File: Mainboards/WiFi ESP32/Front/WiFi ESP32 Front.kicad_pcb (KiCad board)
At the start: 2 copper layers, 71.5 x 24 mm, 8 parts

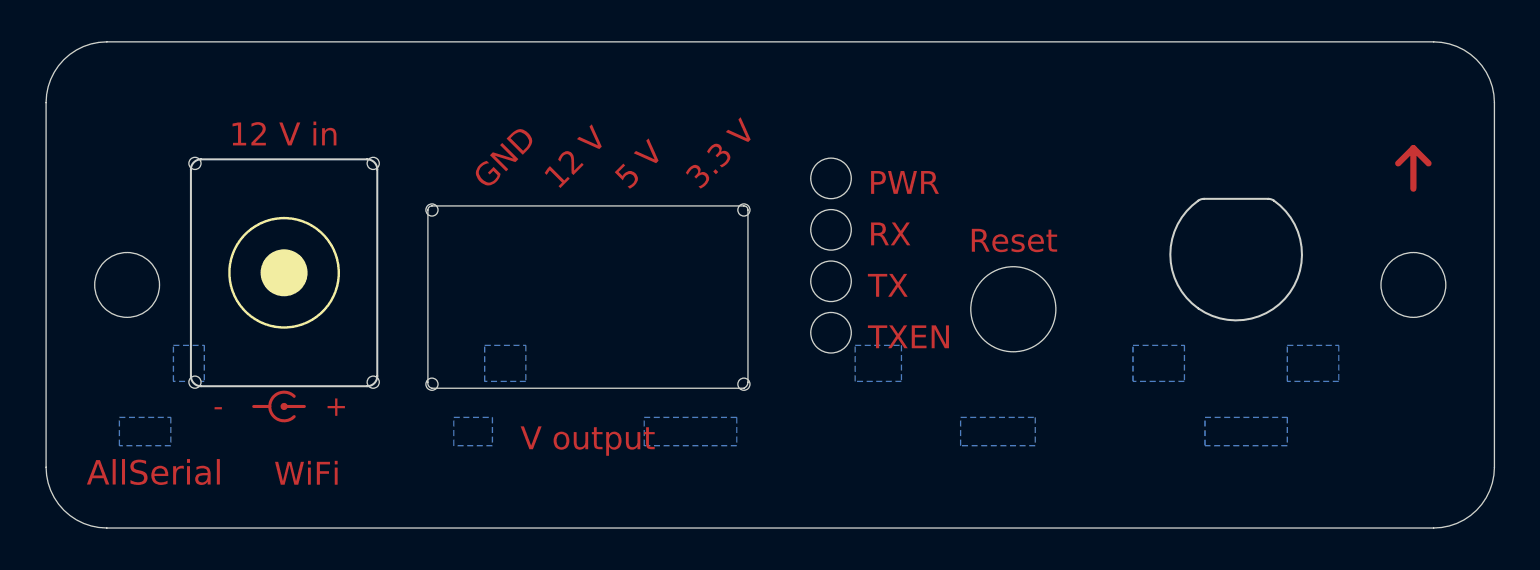
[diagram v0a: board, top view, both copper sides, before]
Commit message: add WiFi Master Front
add symbol lib for fronts
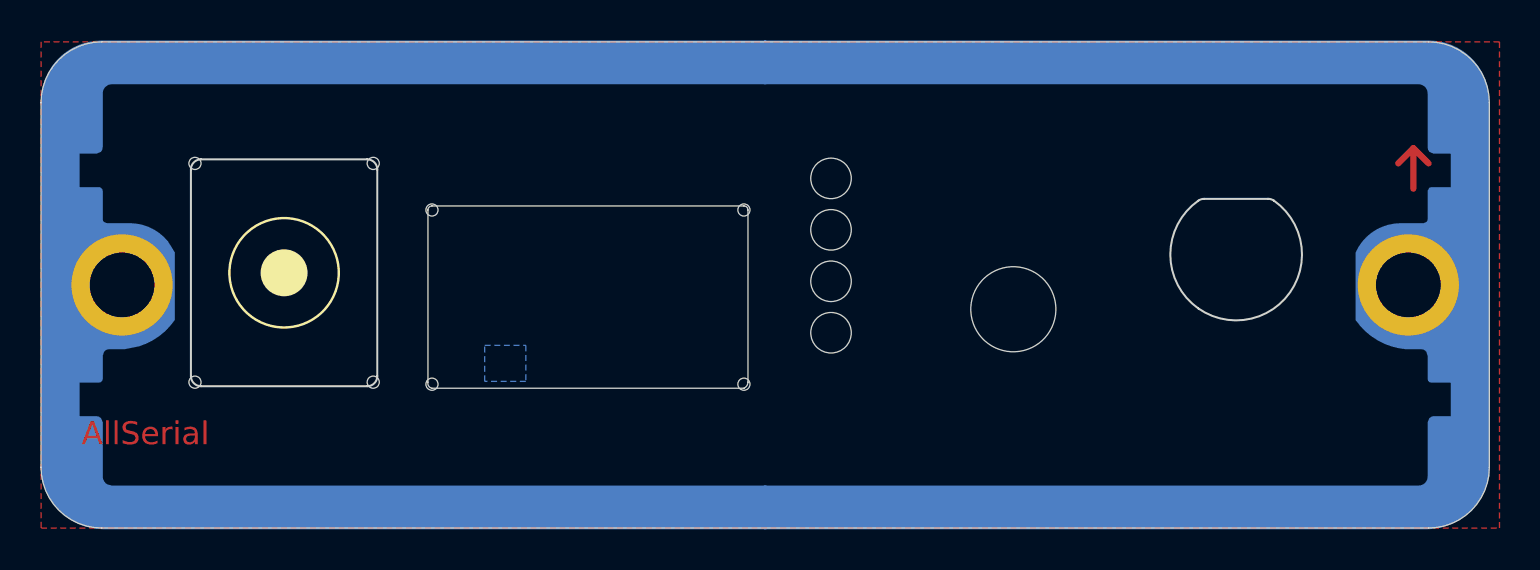
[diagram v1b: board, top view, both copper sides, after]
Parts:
- removed E$3: , AllSerial_Front:Frontpanel_2_Holes
- added U1: ~, AllSerial:Frontpanel_GND_2_Holes_Front, F.Cu at (154.2, 114.7)
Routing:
- added copper zone on B.Cu, net GND
- added copper zone on F.Cu, net GND

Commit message: Migrate to new KiCad Version
Add SMA connector front
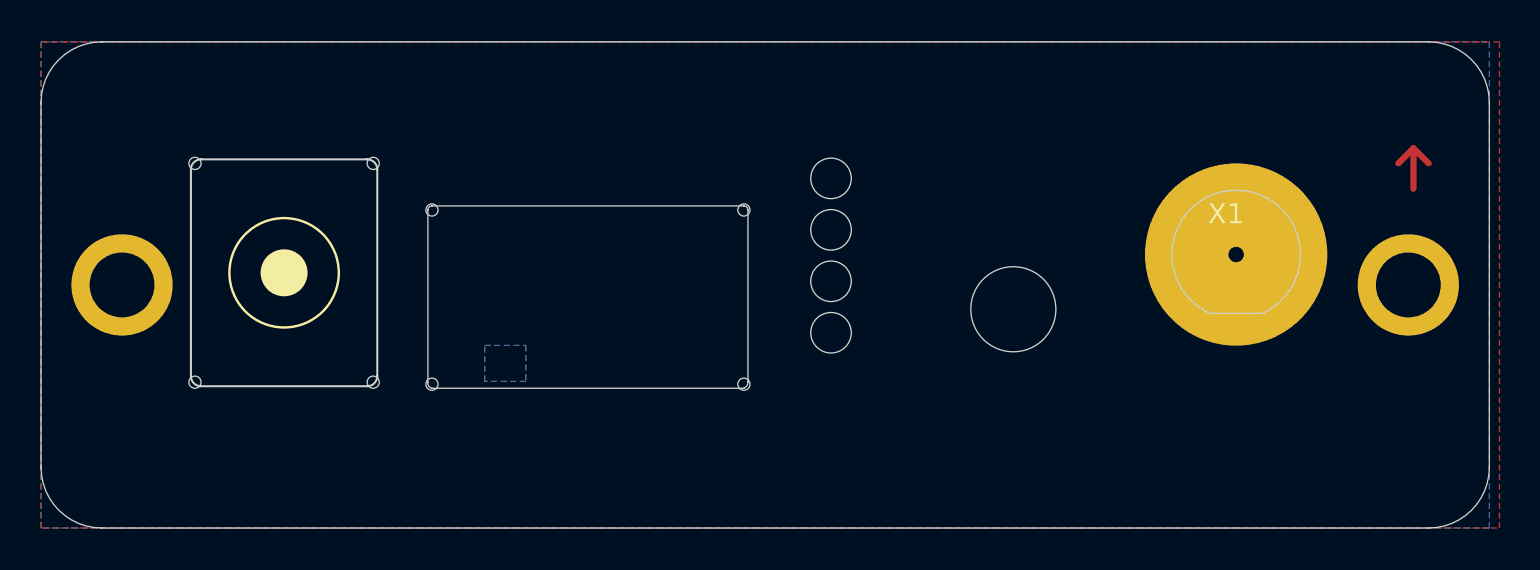
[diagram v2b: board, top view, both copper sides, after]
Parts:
- added ?: , clipboard:195a9c3f-21e4-44ac-8656-a231c8f6a1e0, F.Cu at (142.6, 90.6)
- added X1: ~, AllSerial:SMA-D, F.Cu at (177.4, 101.2)
- U1: footprint AllSerial:Frontpanel_GND_2_Holes_Front -> AllSerial:Frontpanel_GND_2_Holes
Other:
- board text removed: "WiFi"
